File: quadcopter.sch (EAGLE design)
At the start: 77 parts, among them J1 AVR_SPI_PRG_6NS, J3 HEADER-0.1IN-2POS-FEMALE, J4 HEADER-0.1IN-2POS-FEMALE, J5 HEADER-0.1IN-2POS-FEMALE, J6 HEADER-0.1IN-2POS-FEMALE, J8 HEADER-0.1IN-2POS-FEMALE, SW1 PUSHBUTTON_SMD-VERTICAL, SW2 PUSHBUTTON_SMD-VERTICAL, U1 ATMEGA128RFA1

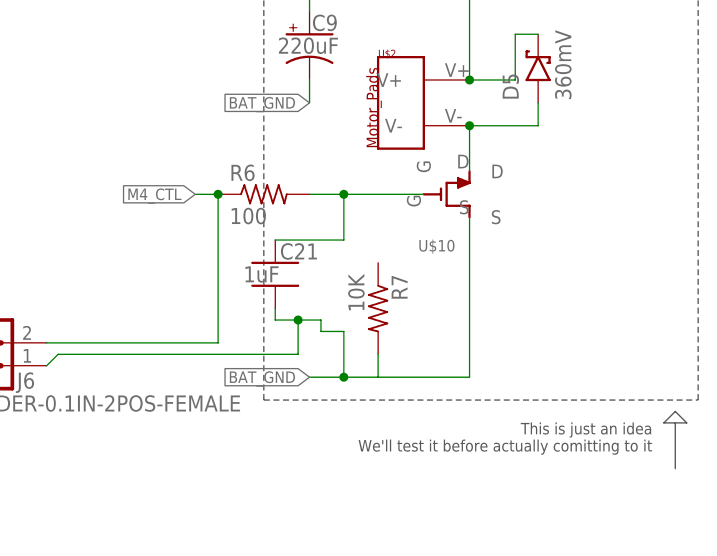
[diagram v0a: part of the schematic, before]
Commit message: Manually routed motors
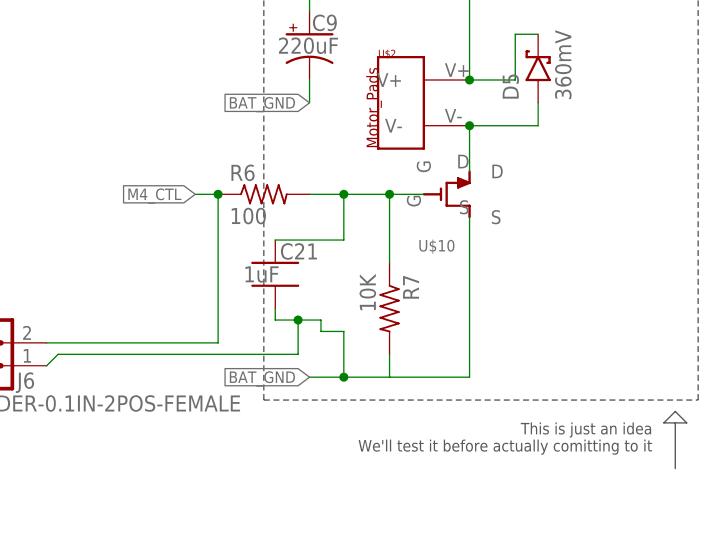
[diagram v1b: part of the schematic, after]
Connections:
- net N$12: now also R7.1
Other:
- moved on the sheet: R7
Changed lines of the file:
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@@
 <instance part="GND12" gate="1" x="248.92" y="-144.78"/>
 <instance part="R6" gate="G$1" x="351.79" y="-203.2"/>
-<instance part="R7" gate="G$1" x="364.49" y="-215.9" rot="R270"/>
+<instance part="R7" gate="G$1" x="365.76" y="-215.9" rot="R270"/>
 <instance part="U$2" gate="G$1" x="367.03" y="-195.58"/>
 <instance part="R4" gate="G$1" x="354.33" y="-160.02"/>
@@
 <pinref part="U$10" gate="G$1" pin="S"/>
 <wire x1="374.65" y1="-205.74" x2="374.65" y2="-223.52" width="0.1524" layer="91"/>
-<wire x1="374.65" y1="-223.52" x2="364.49" y2="-223.52" width="0.1524" layer="91"/>
+<wire x1="374.65" y1="-223.52" x2="365.76" y2="-223.52" width="0.1524" layer="91"/>
 <pinref part="R7" gate="G$1" pin="2"/>
 <wire x1="356.87" y1="-223.52" x2="360.68" y2="-223.52" width="0.1524" layer="91"/>
-<wire x1="360.68" y1="-223.52" x2="364.49" y2="-223.52" width="0.1524" layer="91"/>
-<wire x1="364.49" y1="-223.52" x2="364.49" y2="-220.98" width="0.1524" layer="91"/>
+<wire x1="360.68" y1="-223.52" x2="365.76" y2="-223.52" width="0.1524" layer="91"/>
+<wire x1="365.76" y1="-223.52" x2="365.76" y2="-220.98" width="0.1524" layer="91"/>
 <wire x1="360.68" y1="-218.44" x2="360.68" y2="-223.52" width="0.1524" layer="91"/>
 <junction x="360.68" y="-223.52"/>
@@
 <pinref part="U$10" gate="G$1" pin="G"/>
 <pinref part="C21" gate="G$1" pin="1"/>
-<wire x1="360.68" y1="-203.2" x2="369.57" y2="-203.2" width="0.1524" layer="91"/>
+<wire x1="360.68" y1="-203.2" x2="365.76" y2="-203.2" width="0.1524" layer="91"/>
+<wire x1="365.76" y1="-203.2" x2="369.57" y2="-203.2" width="0.1524" layer="91"/>
 <wire x1="353.06" y1="-208.28" x2="360.68" y2="-208.28" width="0.1524" layer="91"/>
 <wire x1="360.68" y1="-208.28" x2="360.68" y2="-203.2" width="0.1524" layer="91"/>
 <junction x="360.68" y="-203.2"/>
-</segment>
-</net>
+<wire x1="365.76" y1="-210.82" x2="365.76" y2="-203.2" width="0.1524" layer="91"/>
+<junction x="365.76" y="-203.2"/>
+<pinref part="R7" gate="G$1" pin="1"/>
+</segment>
+</net>

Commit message: changed caps, moving grounds
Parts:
- C18, C19, C20, C21: value 1uF -> 0.1uF; device quadparts_prebuilt:CAPACITOR-NP_SMD-2012-0805_CERAMIC-1UF -> quadparts_prebuilt:CAPACITOR-NP_SMD-2012-0805_CERAMIC-0.1UF
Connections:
- net BAT_GND: now also C16.2
- net GND: no longer C16.2

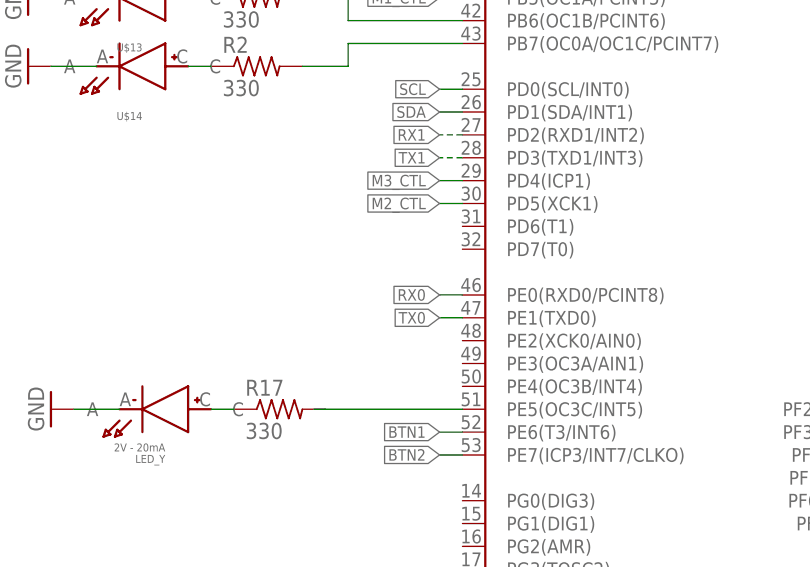
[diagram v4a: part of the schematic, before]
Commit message: remapped and rewired M2_CTL and M3_CTL since the pins they were on were not originally PWM pins
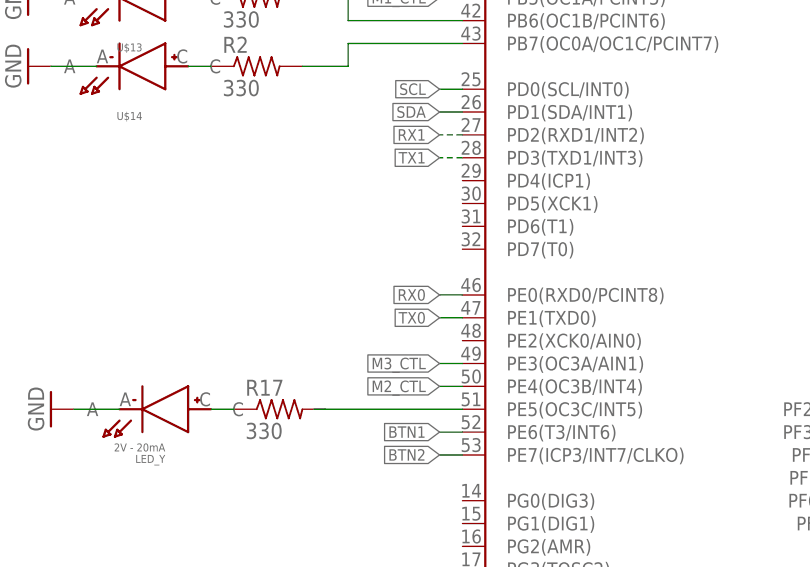
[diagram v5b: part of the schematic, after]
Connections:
- net M2_CTL: now also U1.PE4(OC3B/INT4); no longer U1.PD5(XCK1)
- net M3_CTL: now also U1.PE3(OC3A/AIN1); no longer U1.PD4(ICP1)
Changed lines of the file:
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@@
 <?xml version="1.0" encoding="utf-8"?>
 <!DOCTYPE eagle SYSTEM "eagle.dtd">
-<eagle version="7.6.0">
+<eagle version="8.1.1">
 <drawing>
 <settings>
@@
 <grid distance="0.1" unitdist="inch" unit="inch" style="lines" multiple="1" display="no" altdistance="0.01" altunitdist="inch" altunit="inch"/>
 <layers>
-<layer number="1" name="Top" color="4" fill="1" visible="yes" active="no"/>
-<layer number="2" name="Route2" color="1" fill="3" visible="yes" active="no"/>
-<layer number="3" name="Route3" color="4" fill="3" visible="yes" active="no"/>
-<layer number="4" name="Route4" color="1" fill="4" visible="yes" active="no"/>
-<layer number="5" name="Route5" color="4" fill="4" visible="yes" active="no"/>
-<layer number="6" name="Route6" color="1" fill="8" visible="yes" active="no"/>
-<layer number="7" name="Route7" color="4" fill="8" visible="yes" active="no"/>
-<layer number="8" name="Route8" color="1" fill="2" visible="yes" active="no"/>
-<layer number="9" name="Route9" color="4" fill="2" visible="yes" active="no"/>
-<layer number="10" name="Route10" color="1" fill="7" visible="yes" active="no"/>
-<layer number="11" name="Route11" color="4" fill="7" visible="yes" active="no"/>
-<layer number="12" name="Route12" color="1" fill="5" visible="yes" active="no"/>
-<layer number="13" name="Route13" color="4" fill="5" visible="yes" active="no"/>
-<layer number="14" name="Route14" color="1" fill="6" visible="yes" active="no"/>
-<layer number="15" name="Route15" color="4" fill="6" visible="yes" active="no"/>
-<layer number="16" name="Bottom" color="1" fill="1" visible="yes" active="no"/>
-<layer number="17" name="Pads" color="2" fill="1" visible="yes" active="no"/>
-<layer number="18" name="Vias" color="2" fill="1" visible="yes" active="no"/>
-<layer number="19" name="Unrouted" color="6" fill="1" visible="yes" active="no"/>
-<layer number="20" name="Dimension" color="15" fill="1" visible="yes" active="no"/>
-<layer number="21" name="tPlace" color="7" fill="1" visible="yes" active="no"/>
-<layer number="22" name="bPlace" color="7" fill="1" visible="yes" active="no"/>
-<layer number="23" name="tOrigins" color="15" fill="1" visible="yes" active="no"/>
-<layer number="24" name="bOrigins" color="15" fill="1" visible="yes" active="no"/>
-<layer number="25" name="tNames" color="7" fill="1" visible="yes" active="no"/>
-<layer number="26" name="bNames" color="7" fill="1" visible="yes" active="no"/>
-<layer number="27" name="tValues" color="7" fill="1" visible="yes" active="no"/>
-<layer number="28" name="bValues" color="7" fill="1" visible="yes" active="no"/>
+<layer number="1" name="Top" color="4" fill="1" visible="no" active="no"/>
+<layer number="2" name="Route2" color="1" fill="3" visible="no" active="no"/>
+<layer number="3" name="Route3" color="4" fill="3" visible="no" active="no"/>
+<layer number="4" name="Route4" color="1" fill="4" visible="no" active="no"/>
+<layer number="5" name="Route5" color="4" fill="4" visible="no" active="no"/>
+<layer number="6" name="Route6" color="1" fill="8" visible="no" active="no"/>
+<layer number="7" name="Route7" color="4" fill="8" visible="no" active="no"/>
+<layer number="8" name="Route8" color="1" fill="2" visible="no" active="no"/>
+<layer number="9" name="Route9" color="4" fill="2" visible="no" active="no"/>
+<layer number="10" name="Route10" color="1" fill="7" visible="no" active="no"/>
+<layer number="11" name="Route11" color="4" fill="7" visible="no" active="no"/>
+<layer number="12" name="Route12" color="1" fill="5" visible="no" active="no"/>
+<layer number="13" name="Route13" color="4" fill="5" visible="no" active="no"/>
+<layer number="14" name="Route14" color="1" fill="6" visible="no" active="no"/>
+<layer number="15" name="Route15" color="4" fill="6" visible="no" active="no"/>
+<layer number="16" name="Bottom" color="1" fill="1" visible="no" active="no"/>
+<layer number="17" name="Pads" color="2" fill="1" visible="no" active="no"/>
+<layer number="18" name="Vias" color="2" fill="1" visible="no" active="no"/>
+<layer number="19" name="Unrouted" color="6" fill="1" visible="no" active="no"/>
+<layer number="20" name="Dimension" color="15" fill="1" visible="no" active="no"/>
+<layer number="21" name="tPlace" color="7" fill="1" visible="no" active="no"/>
+<layer number="22" name="bPlace" color="7" fill="1" visible="no" active="no"/>
+<layer number="23" name="tOrigins" color="15" fill="1" visible="no" active="no"/>
+<layer number="24" name="bOrigins" color="15" fill="1" visible="no" active="no"/>
+<layer number="25" name="tNames" color="7" fill="1" visible="no" active="no"/>
+<layer number="26" name="bNames" color="7" fill="1" visible="no" active="no"/>
+<layer number="27" name="tValues" color="7" fill="1" visible="no" active="no"/>
+<layer number="28" name="bValues" color="7" fill="1" visible="no" active="no"/>
 <layer number="29" name="tStop" color="7" fill="3" visible="no" active="no"/>
 <layer number="30" name="bStop" color="7" fill="6" visible="no" active="no"/>
@@
 <layer number="35" name="tGlue" color="7" fill="4" visible="no" active="no"/>
 <layer number="36" name="bGlue" color="7" fill="5" visible="no" active="no"/>
-<layer number="37" name="tTest" color="7" fill="1" visible="yes" active="no"/>
-<layer number="38" name="bTest" color="7" fill="1" visible="yes" active="no"/>
+<layer number="37" name="tTest" color="7" fill="1" visible="no" active="no"/>
+<layer number="38" name="bTest" color="7" fill="1" visible="no" active="no"/>
 <layer number="39" name="tKeepout" color="4" fill="11" visible="no" active="no"/>
 <layer number="40" name="bKeepout" color="1" fill="11" visible="no" active="no"/>
@@
 <layer number="44" name="Drills" color="7" fill="1" visible="no" active="no"/>
 <layer number="45" name="Holes" color="7" fill="1" visible="no" active="no"/>
-<layer number="46" name="Milling" color="3" fill="1" visible="yes" active="no"/>
-<layer number="47" name="Measures" color="7" fill="1" visible="yes" active="no"/>
-<layer number="48" name="Document" color="7" fill="1" visible="yes" active="no"/>
-<layer number="49" name="Reference" color="7" fill="1" visible="yes" active="no"/>
-<layer number="50" name="dxf" color="7" fill="1" visible="yes" active="no"/>
-<layer number="51" name="tDocu" color="7" fill="1" visible="yes" active="no"/>
-<layer number="52" name="bDocu" color="7" fill="1" visible="yes" active="no"/>
-<layer number="53" name="tGND_GNDA" color="7" fill="1" visible="yes" active="no"/>
-<layer number="54" name="bGND_GNDA" color="7" fill="1" visible="yes" active="no"/>
-<layer number="56" name="wert" color="7" fill="1" visible="yes" active="no"/>
-<layer number="57" name="tCAD" color="7" fill="1" visible="yes" active="no"/>
-<layer number="59" name="tFaceplate" color="11" fill="1" visible="yes" active="no"/>
-<layer number="60" name="bFaceplate" color="13" fill="1" visible="yes" active="no"/>
+<layer number="46" name="Milling" color="3" fill="1" visible="no" active="no"/>
+<layer number="47" name="Measures" color="7" fill="1" visible="no" active="no"/>
+<layer number="48" name="Document" color="7" fill="1" visible="no" active="no"/>
+<layer number="49" name="Reference" color="7" fill="1" visible="no" active="no"/>
+<layer number="50" name="dxf" color="7" fill="1" visible="no" active="no"/>
+<layer number="51" name="tDocu" color="7" fill="1" visible="no" active="no"/>
+<layer number="52" name="bDocu" color="7" fill="1" visible="no" active="no"/>
+<layer number="53" name="tGND_GNDA" color="7" fill="1" visible="no" active="no"/>
+<layer number="54" name="bGND_GNDA" color="7" fill="1" visible="no" active="no"/>
+<layer number="56" name="wert" color="7" fill="1" visible="no" active="no"/>
+<layer number="57" name="tCAD" color="7" fill="1" visible="no" active="no"/>
+<layer number="59" name="tFaceplate" color="11" fill="1" visible="no" active="no"/>
+<layer number="60" name="bFaceplate" color="13" fill="1" visible="no" active="no"/>
 <layer number="90" name="Modules" color="5" fill="1" visible="yes" active="yes"/>
 <layer number="91" name="Nets" color="2" fill="1" visible="yes" active="yes"/>
@@
 </segment>
 <segment>
-<pinref part="U1" gate="G$1" pin="PD4(ICP1)"/>
-<wire x1="187.96" y1="-149.86" x2="185.42" y2="-149.86" width="0.1524" layer="91"/>
-<label x="185.42" y="-149.86" size="1.27" layer="95" font="fixed" rot="MR0" xref="yes"/>
+<label x="185.42" y="-170.18" size="1.27" layer="95" font="fixed" rot="MR0" xref="yes"/>
+</segment>
+<segment>
+<pinref part="U1" gate="G$1" pin="PE3(OC3A/AIN1)"/>
+<wire x1="185.42" y1="-170.18" x2="187.96" y2="-170.18" width="0.1524" layer="91"/>
 </segment>
 </net>
@@
 </segment>
 <segment>
-<pinref part="U1" gate="G$1" pin="PD5(XCK1)"/>
-<wire x1="187.96" y1="-152.4" x2="185.42" y2="-152.4" width="0.1524" layer="91"/>
-<label x="185.42" y="-152.4" size="1.27" layer="95" font="fixed" rot="MR0" xref="yes"/>
-</segment>
-</net>
+<label x="185.42" y="-172.72" size="1.27" layer="95" font="fixed" rot="MR0" xref="yes"/>
+</segment>
+<segment>
+<pinref part="U1" gate="G$1" pin="PE4(OC3B/INT4)"/>
+<wire x1="187.96" y1="-172.72" x2="185.42" y2="-172.72" width="0.1524" layer="91"/>
+</segment>
+</net>

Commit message: renaming parts
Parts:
- renumbered U$7 to IMU
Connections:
- net V_BAT renamed VBAT
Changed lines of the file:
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@@
 <part name="GND14" library="quadparts_prebuilt" deviceset="GND" device=""/>
 <part name="GND15" library="quadparts_prebuilt" deviceset="GND" device=""/>
-<part name="U$7" library="quadparts_michael" deviceset="IMU" device=""/>
+<part name="IMU" library="quadparts_michael" deviceset="IMU" device=""/>
 <part name="GND16" library="quadparts_prebuilt" deviceset="GND" device=""/>
 <part name="P+4" library="quadparts_prebuilt" deviceset="VCC" device=""/>
@@
 <instance part="GND14" gate="1" x="25.4" y="-54.61" rot="R270"/>
 <instance part="GND15" gate="1" x="68.58" y="-34.29" rot="R90"/>
-<instance part="U$7" gate="G$1" x="62.23" y="-213.36"/>
+<instance part="IMU" gate="G$1" x="62.23" y="-213.36"/>
 <instance part="GND16" gate="1" x="44.45" y="-200.66" rot="R270"/>
 <instance part="P+4" gate="VCC" x="34.29" y="-203.2" rot="R90"/>
@@
 <pinref part="GND16" gate="1" pin="GND"/>
 <wire x1="46.99" y1="-200.66" x2="49.53" y2="-200.66" width="0.1524" layer="91"/>
-<pinref part="U$7" gate="G$1" pin="GND"/>
+<pinref part="IMU" gate="G$1" pin="GND"/>
 </segment>
 <segment>
@@
 <segment>
 <pinref part="GND24" gate="1" pin="GND"/>
-<pinref part="U$7" gate="G$1" pin="SDO_M"/>
+<pinref part="IMU" gate="G$1" pin="SDO_M"/>
 <wire x1="77.47" y1="-218.44" x2="74.93" y2="-218.44" width="0.1524" layer="91"/>
 </segment>
@@
 </segment>
 <segment>
-<pinref part="U$7" gate="G$1" pin="VDD"/>
+<pinref part="IMU" gate="G$1" pin="VDD"/>
 <pinref part="P+4" gate="VCC" pin="VCC"/>
 <wire x1="49.53" y1="-203.2" x2="44.45" y2="-203.2" width="0.1524" layer="91"/>
@@
 <wire x1="44.45" y1="-203.2" x2="44.45" y2="-205.74" width="0.1524" layer="91"/>
 <junction x="44.45" y="-203.2"/>
-<pinref part="U$7" gate="G$1" pin="VDDIO"/>
+<pinref part="IMU" gate="G$1" pin="VDDIO"/>
 <wire x1="44.45" y1="-205.74" x2="49.53" y2="-205.74" width="0.1524" layer="91"/>
 <wire x1="44.45" y1="-203.2" x2="39.37" y2="-203.2" width="0.1524" layer="91"/>
@@
 <pinref part="P+6" gate="VCC" pin="VCC"/>
 <wire x1="92.71" y1="-215.9" x2="92.71" y2="-220.98" width="0.1524" layer="91"/>
-<pinref part="U$7" gate="G$1" pin="SDO_A/G"/>
+<pinref part="IMU" gate="G$1" pin="SDO_A/G"/>
 <wire x1="92.71" y1="-220.98" x2="74.93" y2="-220.98" width="0.1524" layer="91"/>
 <junction x="92.71" y="-215.9"/>
-<pinref part="U$7" gate="G$1" pin="CS_A/G"/>
+<pinref part="IMU" gate="G$1" pin="CS_A/G"/>
 <wire x1="92.71" y1="-215.9" x2="74.93" y2="-215.9" width="0.1524" layer="91"/>
 <wire x1="92.71" y1="-215.9" x2="92.71" y2="-213.36" width="0.1524" layer="91"/>
-<pinref part="U$7" gate="G$1" pin="CS_M"/>
+<pinref part="IMU" gate="G$1" pin="CS_M"/>
 <wire x1="92.71" y1="-213.36" x2="74.93" y2="-213.36" width="0.1524" layer="91"/>
-<pinref part="U$7" gate="G$1" pin="DEN_A/G"/>
+<pinref part="IMU" gate="G$1" pin="DEN_A/G"/>
 <wire x1="74.93" y1="-200.66" x2="92.71" y2="-200.66" width="0.1524" layer="91"/>
 <wire x1="92.71" y1="-200.66" x2="92.71" y2="-213.36" width="0.1524" layer="91"/>
@@
 </segment>
 </net>
-<net name="V_BAT" class="1">
+<net name="VBAT" class="1">
 <segment>
 <wire x1="367.03" y1="-129.54" x2="367.03" y2="-132.08" width="0.1524" layer="91"/>
@@
 </segment>
 <segment>
-<pinref part="U$7" gate="G$1" pin="SCL/SPC"/>
+<pinref part="IMU" gate="G$1" pin="SCL/SPC"/>
 <wire x1="74.93" y1="-226.06" x2="80.01" y2="-226.06" width="0.1524" layer="91"/>
 <label x="82.55" y="-226.06" size="1.27" layer="95" font="fixed" xref="yes"/>
@@
 </segment>
 <segment>
-<pinref part="U$7" gate="G$1" pin="SDA/SDA/SDO"/>
+<pinref part="IMU" gate="G$1" pin="SDA/SDA/SDO"/>
 <wire x1="74.93" y1="-223.52" x2="96.52" y2="-223.52" width="0.1524" layer="91"/>
 <label x="104.14" y="-223.52" size="1.27" layer="95" font="fixed" xref="yes"/>
@@
 <segment>
 <pinref part="C8" gate="G$1" pin="1"/>
-<pinref part="U$7" gate="G$1" pin="C1"/>
+<pinref part="IMU" gate="G$1" pin="C1"/>
 <wire x1="44.45" y1="-210.82" x2="49.53" y2="-210.82" width="0.1524" layer="91"/>
 </segment>
@@
 <net name="N$14" class="0">
 <segment>
-<pinref part="U$7" gate="G$1" pin="CAP"/>
+<pinref part="IMU" gate="G$1" pin="CAP"/>
 <pinref part="C14" gate="G$1" pin="1"/>
 <wire x1="49.53" y1="-208.28" x2="31.75" y2="-208.28" width="0.1524" layer="91"/>
